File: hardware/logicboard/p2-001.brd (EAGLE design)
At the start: 72 x 72 mm, 30 parts, among them IC1 5V, IC2 74LS07N, IC3 4066N, K1 G5V1, T1 2SC1815, U1 DS18B20

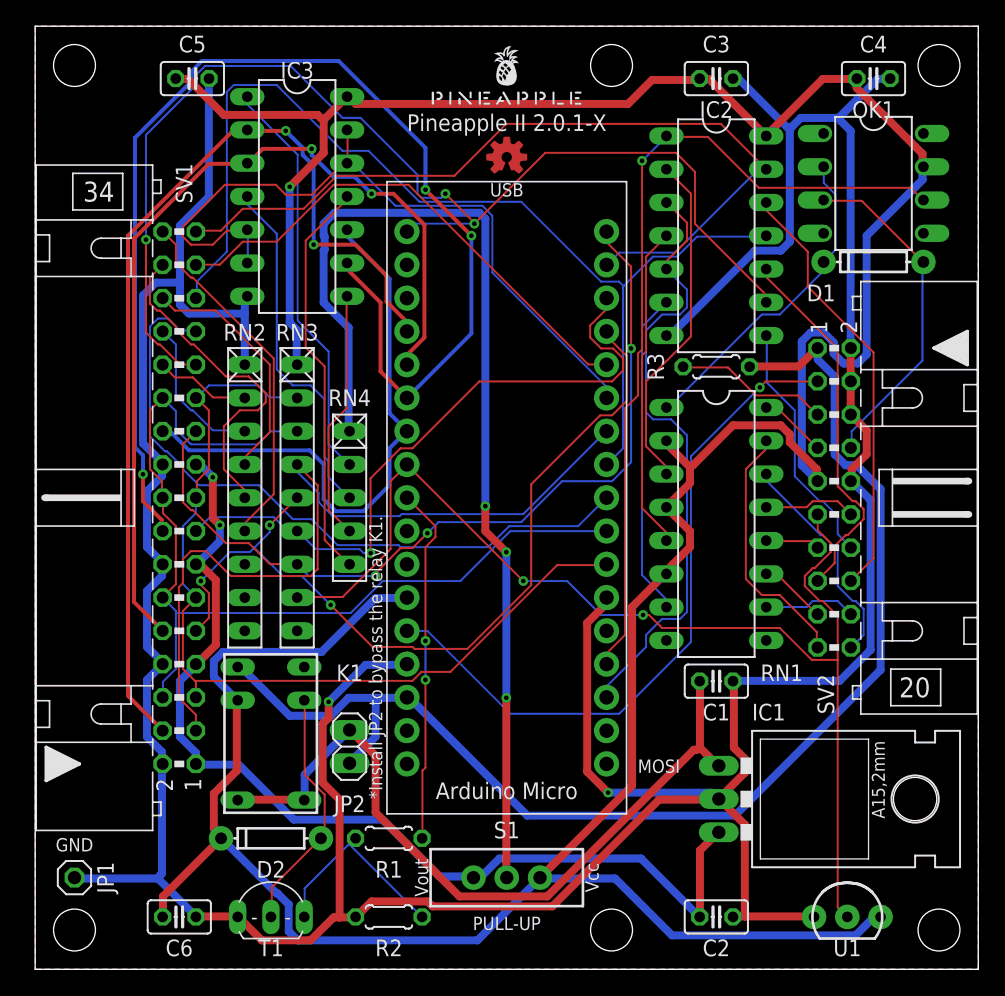
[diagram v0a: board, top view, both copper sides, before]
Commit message: Added RS-422 TX driver.
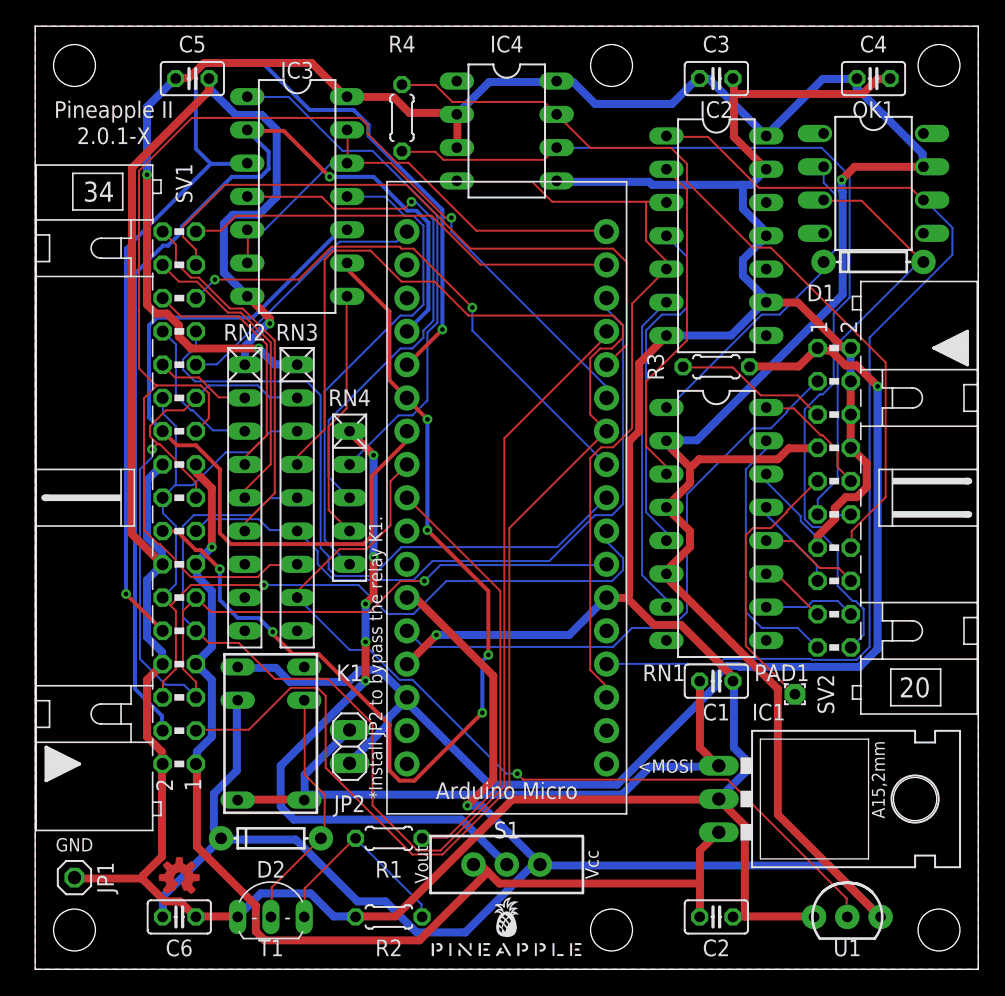
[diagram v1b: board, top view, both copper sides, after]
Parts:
- added IC4: LTC485N, linear-technology:DIL08
- added PAD1: (no value), wirepad:1,6/0,8
- added R4: 120, resistor:0204/5
- moved U$1 65.0 mm to (36.0, 1.00)
- moved LOGO1 60.4 mm to (11.0, 7.00)
- moved S1 1.00 mm to (36.0, 8.00)
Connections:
- net LED0K renamed L0K
- net LED1 renamed L1
- net LED1K renamed L1K
- net LED2K renamed L2K
- net LED3 renamed L3
- net LED3K renamed L3K
- net LED4K renamed L4K
- removed net LED0: IC2.9, MC1.P$34, SV1.25
- removed net LED2: IC2.11, MC1.P$8, SV1.29
- removed net LED4: IC2.13, MC1.P$2, SV1.33
- removed net XLEDB: IC2.10, SV2.15
- removed net XLEDG: IC2.8, SV2.14
- removed net XLEDR: IC2.12, SV2.16
- new net L0: MC1.P$34, SV1.25
- new net L2: MC1.P$8, SV1.29
- new net L4: MC1.P$2, SV1.33
- new net MTX+: IC4.6, R4.1, SV2.12
- new net MTX-: IC4.7, R4.2, SV2.14
- new net N$1: PAD1.1, SV2.9
- net GND: now also IC2.11, IC2.13, IC2.9, IC4.5, SV2.13, SV2.8; no longer SV2.10
- net MINRTN: now also SV2.11; no longer SV2.8
- net MINSND: now also SV2.10; no longer SV2.7
- net MO1RTN: now also SV2.16; no longer SV2.13
- net MO1SND: now also SV2.15; no longer SV2.12
- net THS: no longer SV2.11
- net TX: now also IC4.4
- net VCC: now also IC4.2, IC4.3, IC4.8, SV2.7; no longer SV2.9
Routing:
- net LED0: track 91.1 -> 0.00 mm, vias 3 -> 0
- net LED2: track 80.3 -> 0.00 mm
- net MTX+: track 0.00 -> 67.7 mm
- net LED4: track 63.6 -> 0.00 mm
- net MTX-: track 0.00 -> 61.8 mm
- net D1: track 62.6 -> 118.3 mm
- net L2: track 0.00 -> 40.9 mm, vias 0 -> 2
- net L4: track 0.00 -> 33.4 mm
- net XLEDR: track 33.0 -> 0.00 mm
- net VPULLUP: track 80.6 -> 51.4 mm, vias 3 -> 5
- net XLEDB: track 28.6 -> 0.00 mm
- net D2: track 64.7 -> 92.2 mm, vias 3 -> 0
- net D4: track 64.5 -> 91.0 mm, vias 3 -> 0
- net VCC: track 274.9 -> 297.4 mm, vias 1 -> 4
- net N$1: track 0.00 -> 21.0 mm
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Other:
- board text added: "2.0.1-X"
- board text added: "<MOSI"
- board text added: "Pineapple II"
- board text removed: "MOSI"
- board text removed: "PULL-UP"
- board text removed: "Pineapple II 2.0.1-X"
- board text removed: "USB"

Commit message: Fixed unconnected wires.
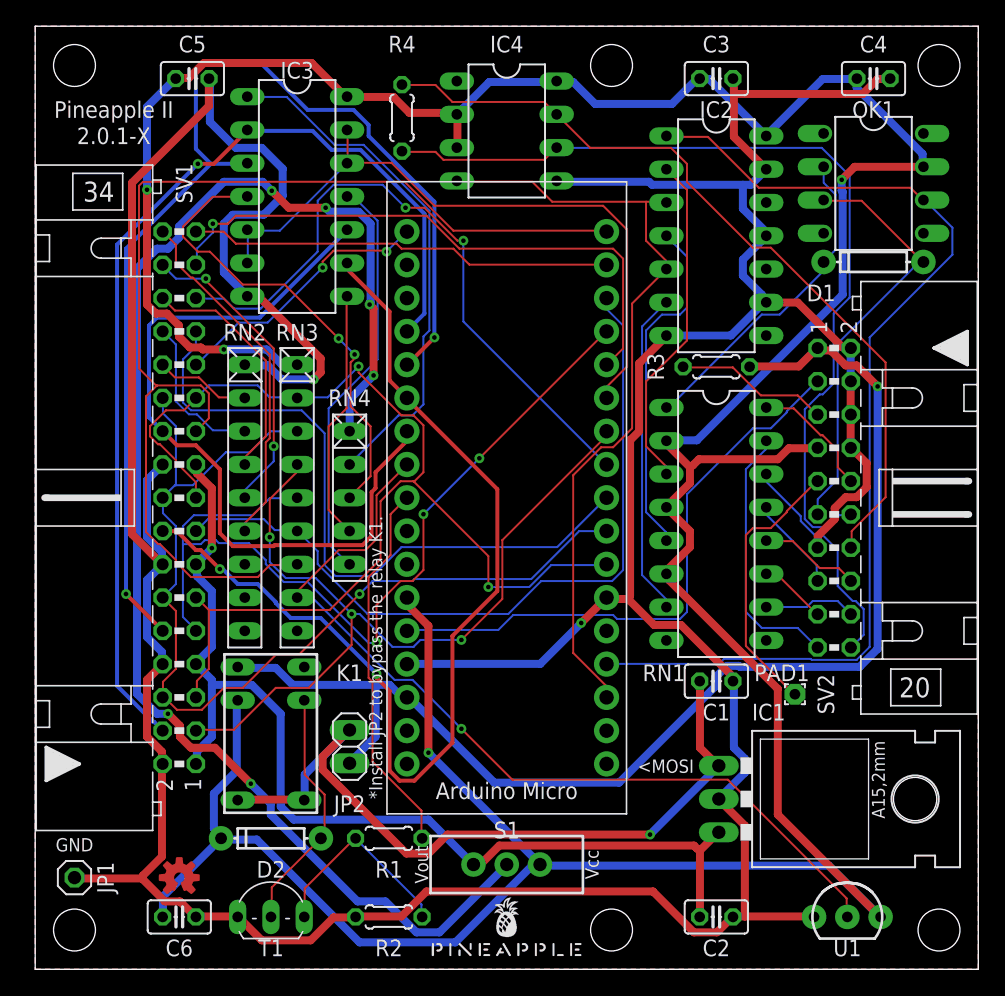
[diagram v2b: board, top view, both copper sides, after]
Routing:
- net VPULLUP: track 51.4 -> 110.5 mm, vias 5 -> 6
- net D1: track 118.3 -> 63.3 mm, vias 0 -> 3
- net D2: track 92.2 -> 68.0 mm, vias 0 -> 3
- net L2: track 40.9 -> 50.3 mm
- net GND: track 321.7 -> 330.5 mm
- net PULLUP: track 43.2 -> 51.9 mm, vias 1 -> 0
- net V+12V: track 51.8 -> 58.6 mm, vias 0 -> 1
- net N$6: track 37.1 -> 31.6 mm
- net N$4: track 41.1 -> 35.8 mm, vias 1 -> 2
- net D4: track 91.0 -> 85.8 mm
- net D3: track 54.2 -> 59.2 mm
- net VOUT: track 85.7 -> 80.8 mm
- net L3: track 49.5 -> 45.3 mm, vias 0 -> 1
- net SDA: track 84.2 -> 88.3 mm
- net RLY: track 32.5 -> 28.9 mm
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
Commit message: Now pin 3 of MIDI In is connected to Vcc.
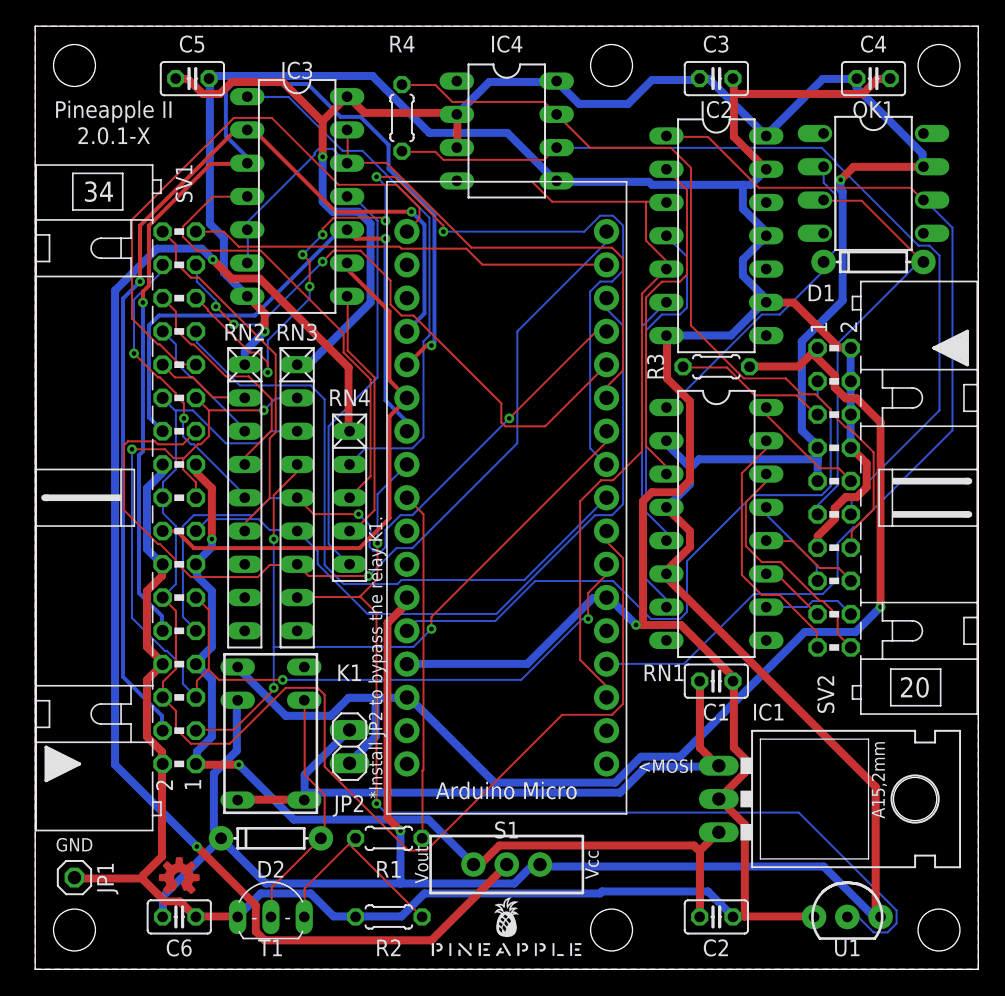
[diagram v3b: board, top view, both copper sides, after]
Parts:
- removed PAD1: (no value), wirepad:1,6/0,8
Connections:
- removed net N$1: PAD1.1, SV2.9
- net VCC: now also SV2.9
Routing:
- net A3: track 77.8 -> 40.7 mm, vias 2 -> 0
- net SCL: track 76.3 -> 102.0 mm, vias 1 -> 0
- net L0: track 20.6 -> 44.1 mm, vias 2 -> 0
- net GND: track 330.5 -> 308.1 mm
- net L2: track 50.3 -> 72.3 mm, vias 2 -> 7
- net N$1: track 21.0 -> 0.00 mm
- net D4: track 85.8 -> 67.3 mm, vias 0 -> 1
- net D2: track 68.0 -> 52.1 mm, vias 3 -> 2
- net VCC: track 295.4 -> 281.0 mm, vias 4 -> 3
- net THS: track 67.7 -> 81.3 mm, vias 1 -> 2
- net A4: track 58.6 -> 45.3 mm, vias 0 -> 1
- net VPULLUP: track 110.5 -> 103.0 mm, vias 6 -> 2
- net V+12V: track 58.6 -> 51.9 mm, vias 1 -> 0
- net VOUT: track 80.8 -> 75.4 mm, vias 1 -> 2
- net RST: track 44.8 -> 50.0 mm
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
